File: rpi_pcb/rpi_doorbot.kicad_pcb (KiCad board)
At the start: 2 copper layers, 29.2 x 51.8 mm, 20 parts, among them J1 Conn_01x07_Male, J2 Conn_01x02_Female, J3 Barrel_Jack, J4 WROOM32_1, J5 WROOM32_2, Q1 ZXMP4A16G, U1 L7805

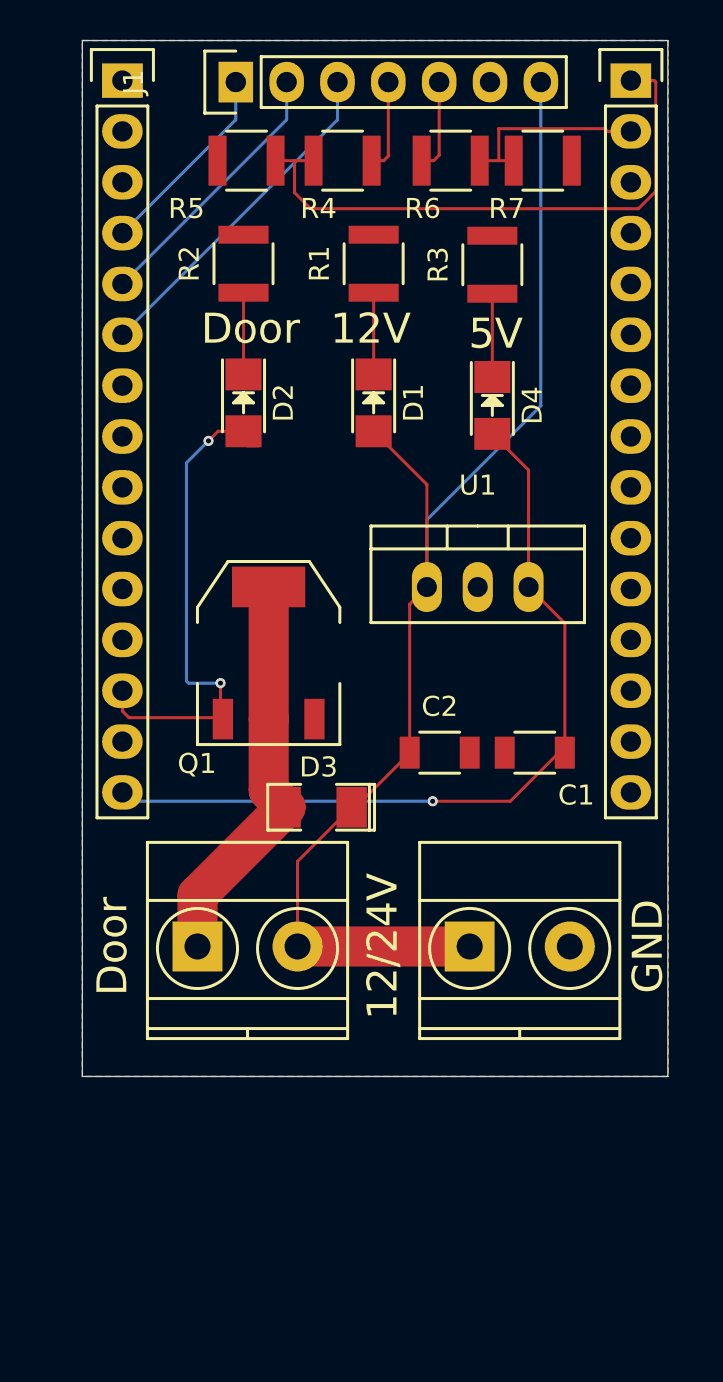
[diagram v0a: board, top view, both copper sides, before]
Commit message: RPi doorbot hat laid out
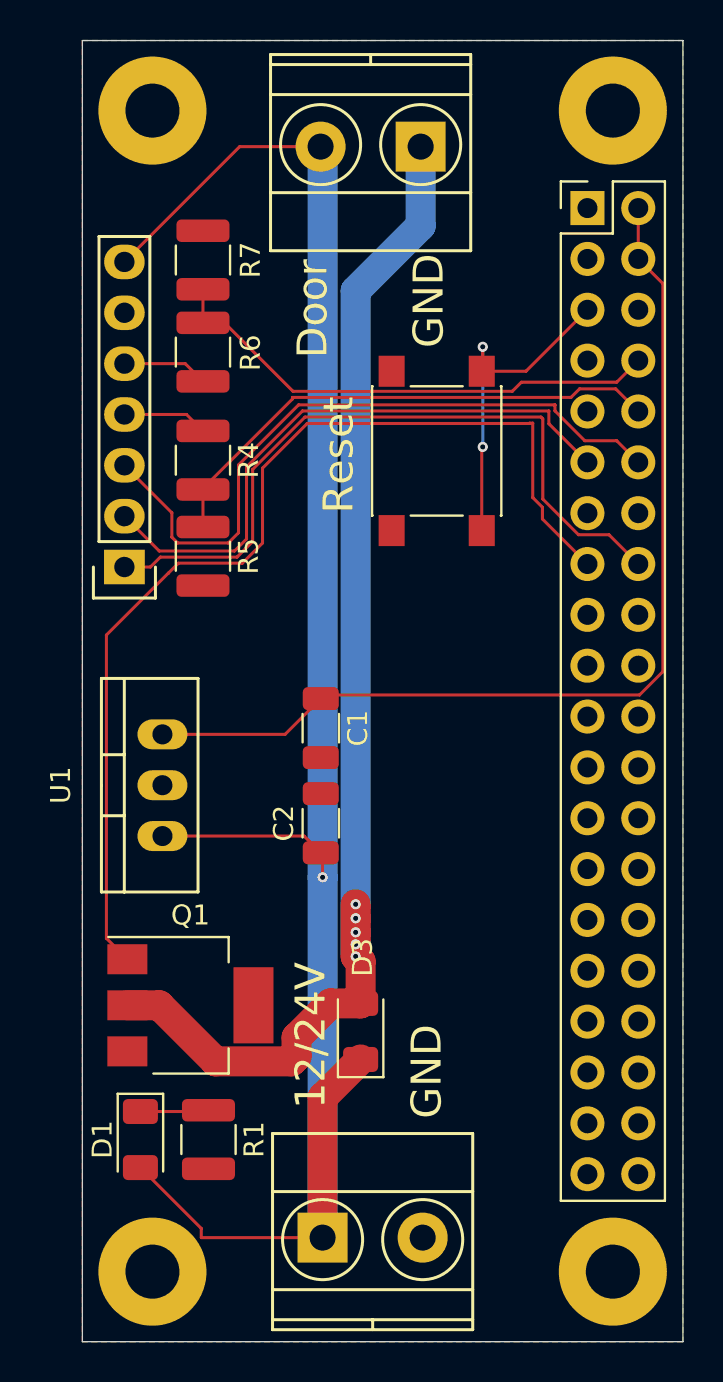
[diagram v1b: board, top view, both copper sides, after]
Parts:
- removed D2, D4: LED, LEDs:LED-1206
- removed J5: WROOM32_2, Pin_Headers:Pin_Header_Straight_1x15
- removed R2, R3: 1K, Resistors_SMD:R_1210
- added H1: MountingHole, MountingHole:MountingHole_2.7mm_M2.5_Pad, F.Cu at (101.5, 101.5)
- added H2: MountingHole, MountingHole:MountingHole_2.7mm_M2.5_Pad, F.Cu at (124.5, 101.5)
- added H3: MountingHole, MountingHole:MountingHole_2.7mm_M2.5_Pad, F.Cu at (101.5, 159.5)
- added H4: MountingHole, MountingHole:MountingHole_2.7mm_M2.5_Pad, F.Cu at (124.5, 159.5)
- added SW1: SW_Push, Button_Switch_SMD:SW_SPST_PTS645, F.Cu at (115.7, 118.5)
- C1, C2: footprint Capacitors_SMD:C_1206 -> Capacitor_SMD:C_1206_3216Metric
- D1: footprint LEDs:LED-1206 -> LED_SMD:LED_1206_3216Metric
- D3: footprint SMD_Packages:SMD-1206_Pol -> Diode_SMD:D_1206_3216Metric
- J4: value WROOM32_1 -> Raspberry_Pi_2_3; footprint Pin_Headers:Pin_Header_Straight_1x15 -> Connector_PinHeader_2.54mm:PinHeader_2x20_P2.54mm_Vertical
- Q1: value ZXMP4A16G -> NDT3055; footprint TO_SOT_Packages_SMD:SOT-223 -> Package_TO_SOT_SMD:SOT-223
- R1, R4, R5, R6, R7: footprint Resistors_SMD:R_1210 -> Resistor_SMD:R_1210_3225Metric
- moved R1 44.5 mm to (104.3, 152.9), turned to -90 degrees
- moved J2 41.5 mm to (114.9, 103.3), turned to 180 degrees
- moved D1 38.6 mm to (100.9, 152.9)
- moved J1 24.9 mm to (100.1, 124.3), turned to 180 degrees
- moved J4 24.1 mm to (123.2, 106.4)
- moved R5 19.9 mm to (104.0, 123.8), turned to -90 degrees
- moved U1 18.6 mm to (102.0, 135.2), turned to 90 degrees
- moved Q1 18.0 mm to (103.4, 146.2)
- moved R7 17.7 mm to (104.0, 109.0), turned to 90 degrees
- moved R4 16.5 mm to (104.0, 119.0), turned to -90 degrees
- moved J3 16.3 mm to (110.0, 157.8)
- moved R6 15.6 mm to (104.0, 113.6), turned to 90 degrees
- moved D3 11.4 mm to (111.9, 147.5), turned to 90 degrees
- moved C1 10.8 mm to (109.9, 132.3), turned to -90 degrees
- moved C2 6.91 mm to (109.9, 137.1), turned to 90 degrees
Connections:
- J4 pad 1: Net-(J4-Pad1) -> unconnected-(J4-Pad1)
- J4 pad 10: Net-(J4-Pad10) -> WIEGAND_OUT2
- J4 pad 11: Net-(J4-Pad11) -> READER_LED
- J4 pad 12: Net-(J4-Pad12) -> READER_BUZZ
- J4 pad 13: DOOR -> unconnected-(J4-Pad13)
- J4 pad 15: 5V -> DOOR
- J4 pad 2: Net-(J4-Pad2) -> 5V
- J4 pad 3: Net-(J4-Pad3) -> unconnected-(J4-Pad3)
- J4 pad 4: 24_32_SWITCH -> 5V
- J4 pad 5: READER_LED -> RESET
- J4 pad 6: READER_BUZZ -> GND
- J4 pad 7: Net-(J4-Pad7) -> unconnected-(J4-Pad7)
- J4 pad 8: Net-(J4-Pad8) -> WIEGAND_OUT1
- J4 pad 9: Net-(J4-Pad9) -> GND
- Q1 pad 4: LATCH_OUT -> (no net)
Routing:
- net LATCH_OUT: track 20.1 -> 62.2 mm, vias 0 -> 5
- net 12V: track 65.7 -> 97.1 mm, vias 0 -> 1
- net DOOR: track 25.0 -> 52.7 mm, vias 2 -> 0
- net 24_32_SWITCH: track 10.4 -> 36.3 mm
- net READER_BUZZ: track 17.1 -> 34.2 mm
- net RESET: track 0.00 -> 17.0 mm, vias 0 -> 2
- net READER_LED: track 13.5 -> 30.3 mm
- net WIEGAND_OUT1: track 9.96 -> 25.5 mm
- net 5V: track 41.0 -> 50.3 mm, vias 1 -> 0
- net Net-(D4-Pad1): track 4.16 -> 0.00 mm
- net Net-(D2-Pad1): track 4.08 -> 0.00 mm
- net WIEGAND_OUT2: track 29.0 -> 26.2 mm
- removed copper zone on B.Cu, net GND
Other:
- board size 29.2 x 51.8 mm -> 30 x 65 mm
- net class Default removed
- board text added: "RPi Doorbot v1 By Timm Murray Copyright © 2024 BY-CC"
- board text added: "Reset"
- board text removed: "12V"
- board text removed: "5V"
- board text removed: "ESP32 Doorbot v5 By Timm Murray Copyright © 2021 BY-CC"
